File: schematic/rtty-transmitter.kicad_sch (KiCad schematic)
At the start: 71 parts, among them J1 USB Type B Connector, J2 USBasp header, J3 2x5 Pin Header Connector Fema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, J4 Conn_01x02_Pin, J5 Conn_01x02_Pin, J6 Conn_01x02_Pin, J7 SMA Vertical Female, Q1 PN2222A, Q2 PN2222A, U1 MCP2221AxP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

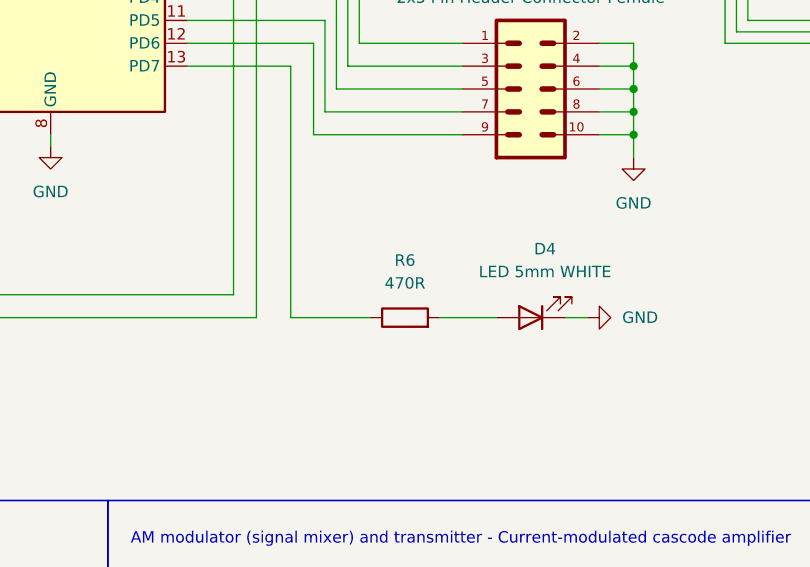
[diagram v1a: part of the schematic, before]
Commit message: White status LED current limiting resistor changed from 470R to 1k
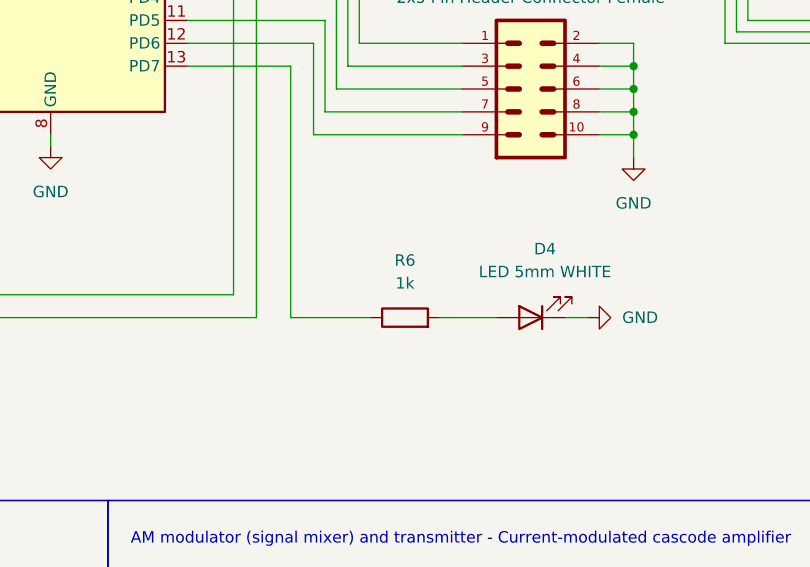
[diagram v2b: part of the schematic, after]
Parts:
- R6: value 470R -> 1k; footprint StockLib:R_470_Axial_DIN0207 -> StockLib:R_1k_Axial_DIN0207
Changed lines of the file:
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@@
 			)
 		)
-		(property "Value" "470R"
+		(property "Value" "1k"
 			(at 171.45 146.05 90)
 			(effects
@@
 			)
 		)
-		(property "Footprint" "StockLib:R_470_Axial_DIN0207"
+		(property "Footprint" "StockLib:R_1k_Axial_DIN0207"
 			(at 171.45 151.638 90)
 			(effects

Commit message: Schematic and PCB LED colors updated
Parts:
- D2: footprint StockLib:LED_D5.0mm_YELLOW -> StockLib:LED_D5.0mm_GREEN
- D4: footprint StockLib:LED_D5.0mm_YELLOW -> StockLib:LED_D5.0mm_WHITE
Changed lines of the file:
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@@
 			)
 		)
-		(property "Footprint" "StockLib:LED_D5.0mm_YELLOW"
+		(property "Footprint" "StockLib:LED_D5.0mm_WHITE"
 			(at 185.42 149.86 0)
 			(effects
@@
 			)
 		)
-		(property "Footprint" "StockLib:LED_D5.0mm_YELLOW"
+		(property "Footprint" "StockLib:LED_D5.0mm_GREEN"
 			(at 66.04 139.7 0)
 			(effects
